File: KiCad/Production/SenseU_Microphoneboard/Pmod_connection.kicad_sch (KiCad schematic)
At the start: 8 parts, among them J1 90122-0126

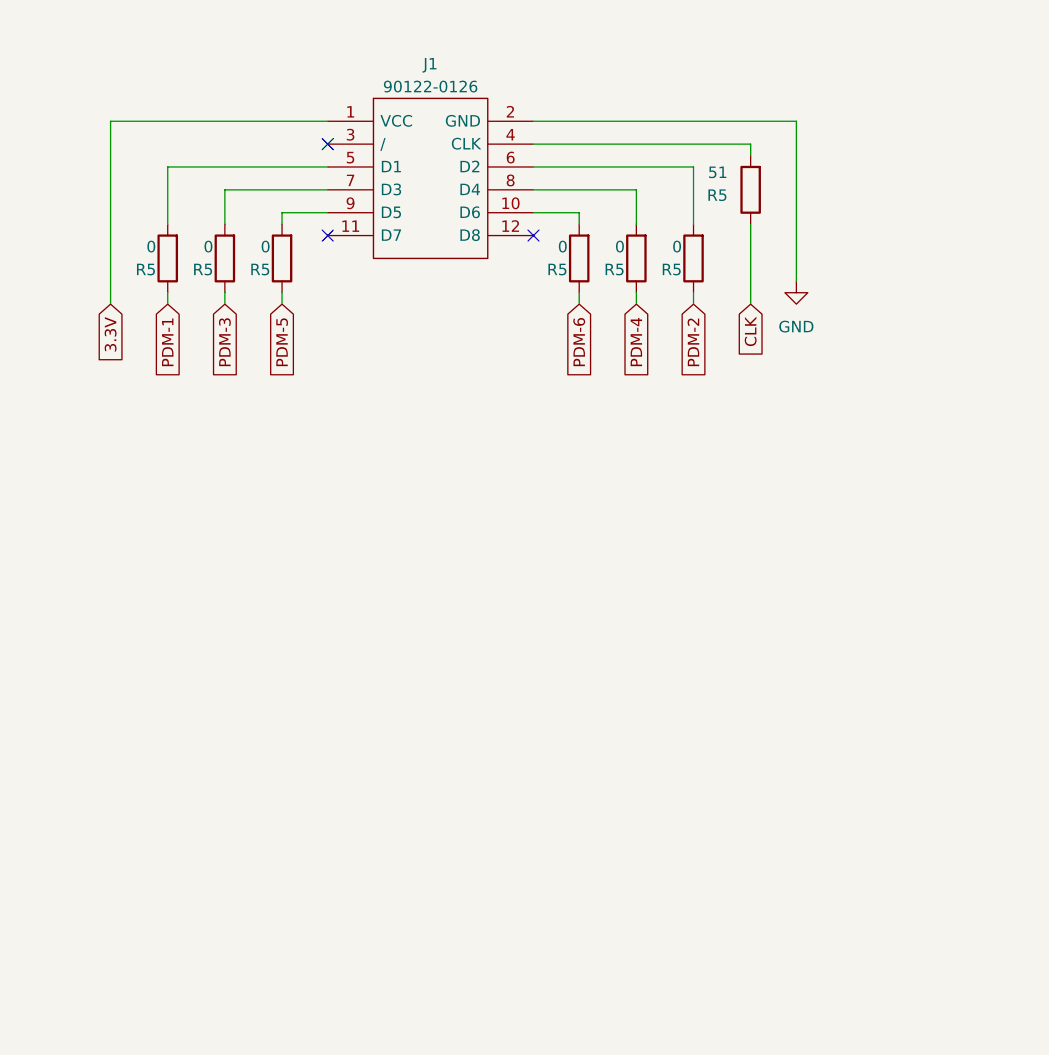
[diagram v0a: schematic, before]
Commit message: PCB V1 finished (9 MEMS), DRC violation rules pending
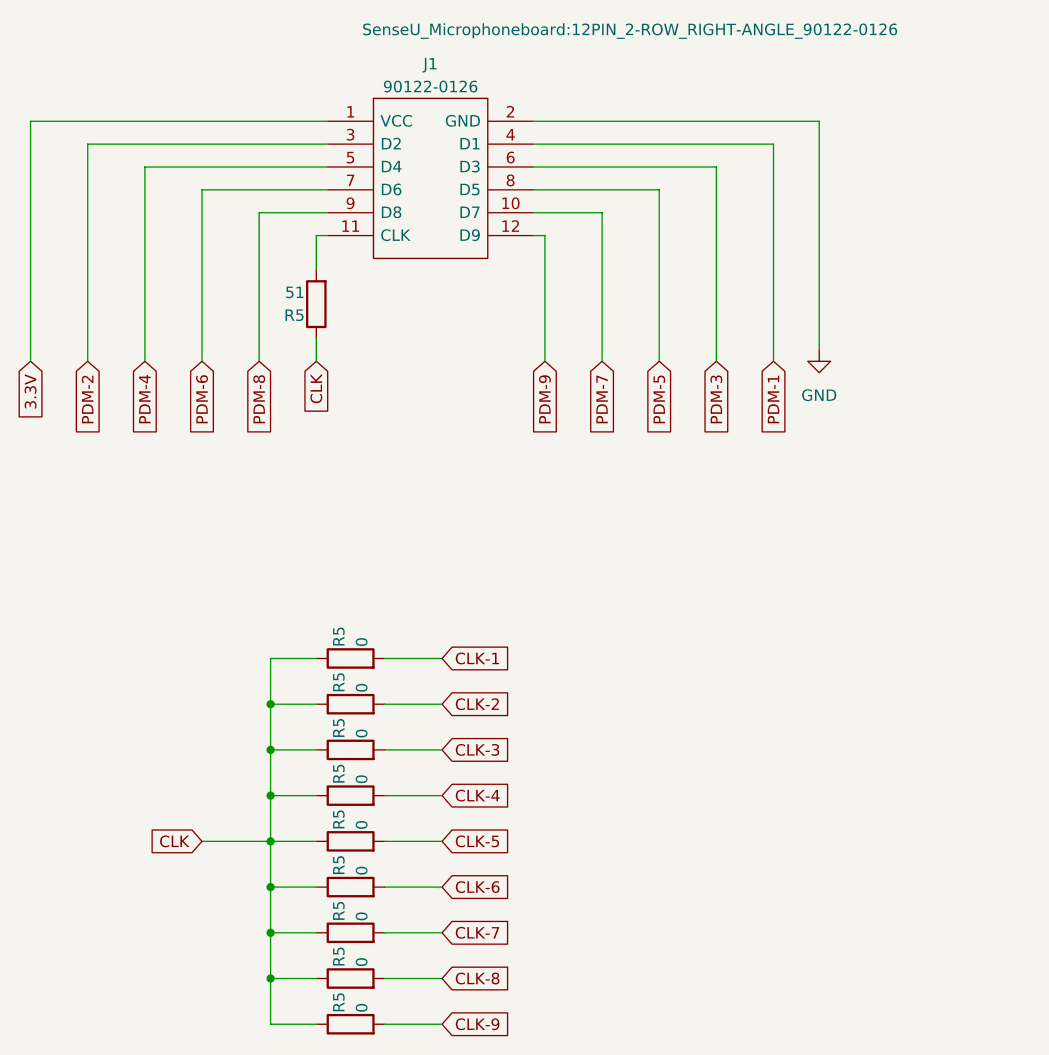
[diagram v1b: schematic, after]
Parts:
- removed R5: 51, Resistor_SMD:R_0603_1608Metric_Pad0.98x0.95mm_HandSolder, symbol Device:R
- removed R5 (x6): 0, Resistor_SMD:R_0603_1608Metric_Pad0.98x0.95mm_HandSolder, symbol Device:R
- added R5 (x9): 0, Resistor_SMD:R_0603_1608Metric_Pad0.98x0.95mm_HandSolder, symbol Device:R
- added R5: 51, Resistor_SMD:R_0603_1608Metric_Pad0.98x0.95mm_HandSolder, symbol Device:R
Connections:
- net CLK: now also R5.1, R5.1, R5.1, R5.1, R5.1, R5.1, R5.1, R5.1, R5.1, R5.1
- net PDM-1: now also J1.4 (D1)
- net PDM-2: now also J1.3 (D2)
- net PDM-3: now also J1.6 (D3)
- net PDM-4: now also J1.5 (D4)
- net PDM-5: now also J1.8 (D5)
- net PDM-6: now also J1.7 (D6)
- net PDM-8: now reaches J1.9 (D8)
- net PDM-7: now reaches J1.10 (D7)
- net at J1.11 (CLK): now also R5.2
- net PDM-9: now reaches J1.12 (D9)
- new net CLK-1: R5.2
- new net CLK-2: R5.2
- new net CLK-3: R5.2
- new net CLK-4: R5.2
- new net CLK-5: R5.2
- new net CLK-6: R5.2
- new net CLK-7: R5.2
- new net CLK-8: R5.2
- new net CLK-9: R5.2
- no-connect marks 3 -> 0
